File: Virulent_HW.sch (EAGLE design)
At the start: 6 parts

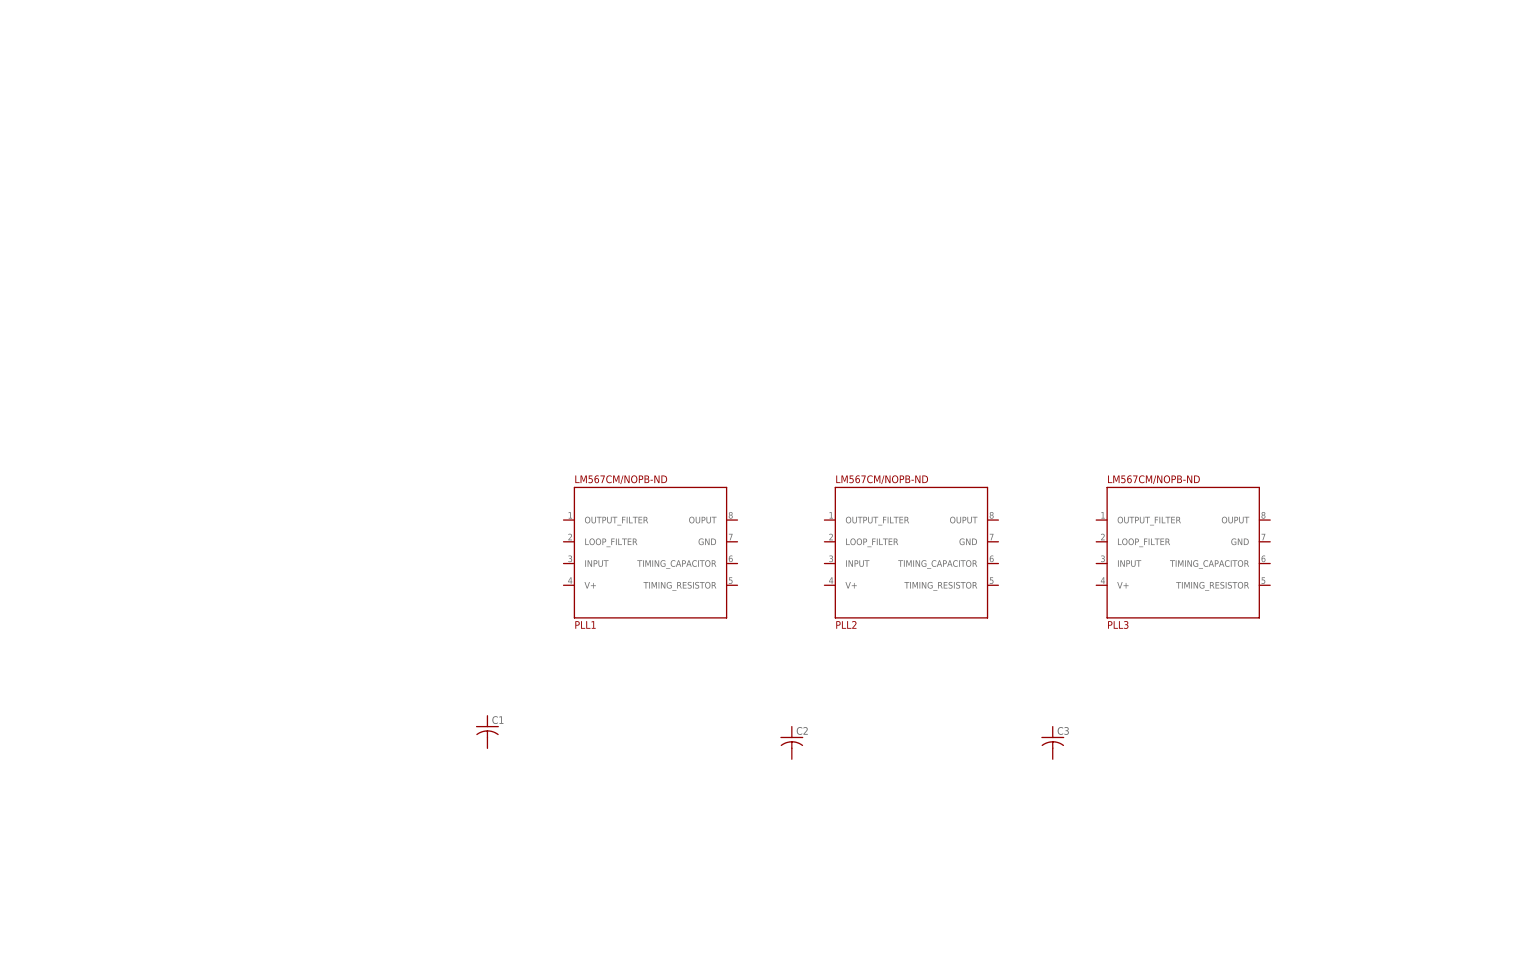
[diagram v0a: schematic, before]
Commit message: Added datasheets folder. Added power supply to schematic.
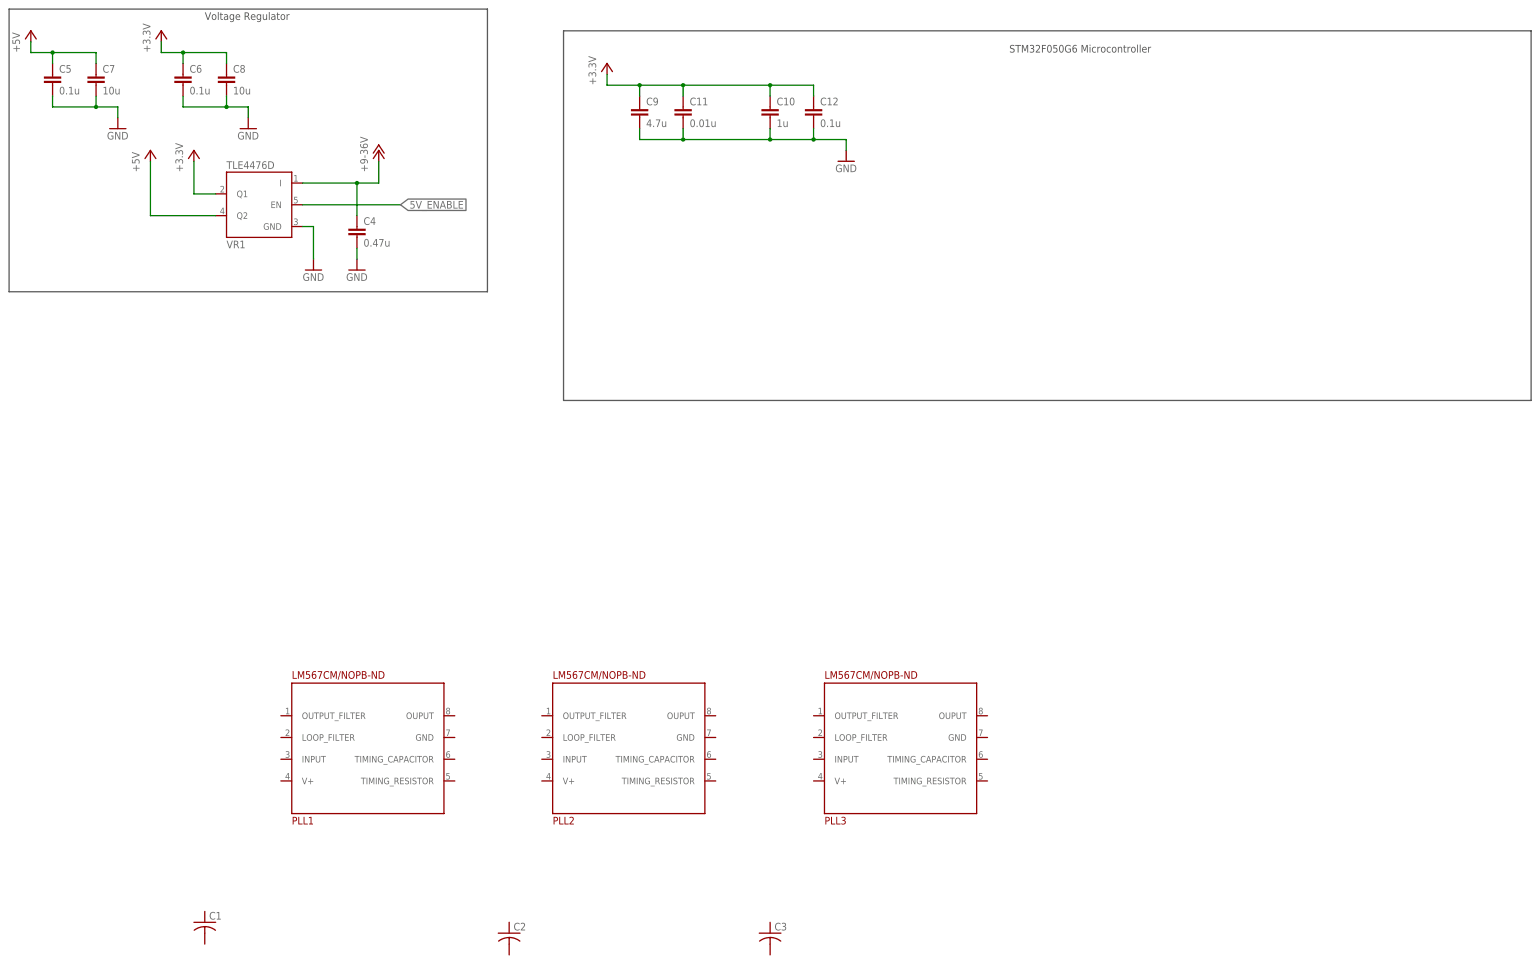
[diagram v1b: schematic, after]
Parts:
- added C10: 1u, rcl:C-EUC0805
- added C11: 0.01u, rcl:C-EUC0402
- added C12, C5, C6: 0.1u, rcl:C-EUC0402
- added C4: 0.47u, rcl:C-EUC1206
- added C7, C8: 10u, rcl:C-EUC1206
- added C9: 4.7u, rcl:C-EUC0805
- added VR1: TLE4476D, motorFeedback:TLE4476D
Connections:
- new net +3.3V: C10.1, C11.1, C12.1, C6.1, C8.1, C9.1, VR1.Q1@2
- new net +5V: C5.1, C7.1, VR1.Q2@4
- new net +9-36V: C4.1, VR1.I@1
- new net 5V_ENABLE: VR1.EN@5
- new net GND: C10.2, C11.2, C12.2, C4.2, C5.2, C6.2, C7.2, C8.2, C9.2, VR1.GND@3
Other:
- note added: "STM32F050G6 Microcontroller"
- note added: "Voltage Regulator"
- moved on the sheet: C1, C2, C3, PLL1, PLL2, PLL3

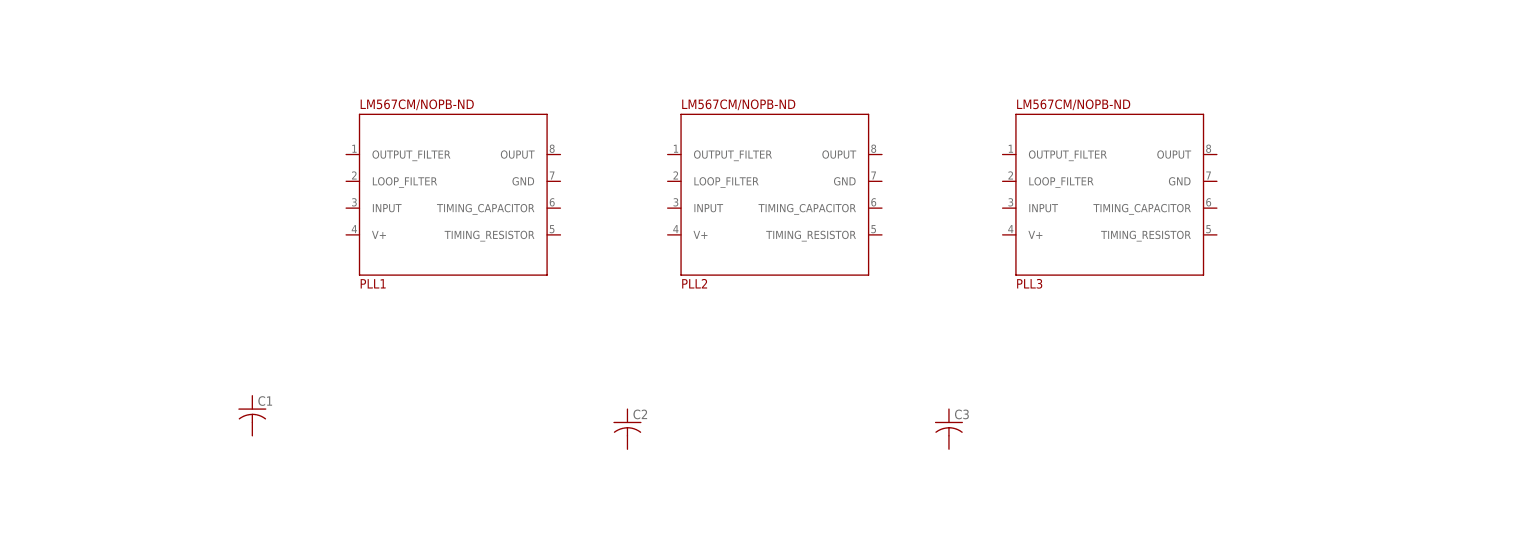
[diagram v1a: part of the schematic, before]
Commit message: Added RGB LED (MSL0201RGB) and Hex Inverter (SN74ACT14) to library. Updated PLL circuitry in schematic.
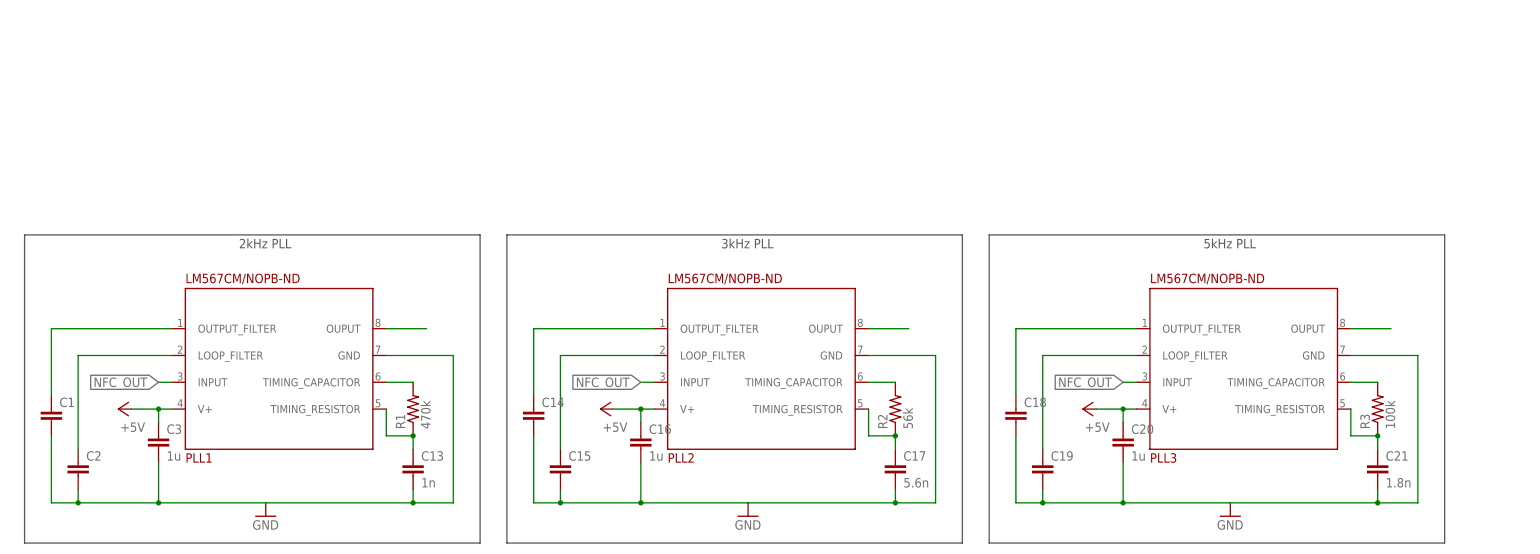
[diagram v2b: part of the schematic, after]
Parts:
- added C13: 1n, rcl:C-EUC1206
- added C14, C15, C18, C19: (no value), rcl:C-EUC1206
- added C16, C20: 1u, rcl:C-EUC1206
- added C17: 5.6n, rcl:C-EUC1206
- added C21: 1.8n, rcl:C-EUC1206
- added R1: 470k, Virulent_HW:R-US_R0402
- added R2: 56k, Virulent_HW:R-US_R0402
- added R3: 100k, Virulent_HW:R-US_R0402
- C1, C2: device rcl:C-USC0805 -> rcl:C-EUC1206
- C3: value (none) -> 1u; device rcl:C-USC0805 -> rcl:C-EUC1206
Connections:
- new net N$1: C1.1, PLL1.OUTPUT_FILTER@1
- new net N$10: C17.1, PLL2.TIMING_RESISTOR@5, R2.1
- new net N$12: C18.1, PLL3.OUTPUT_FILTER@1
- new net N$13: PLL3.TIMING_CAPACITOR@6, R3.2
- new net N$14: C19.1, PLL3.LOOP_FILTER@2
- new net N$15: PLL3.OUPUT@8
- new net N$17: C21.1, PLL3.TIMING_RESISTOR@5, R3.1
- new net N$2: C14.1, PLL2.OUTPUT_FILTER@1
- new net N$3: PLL1.TIMING_CAPACITOR@6, R1.2
- new net N$4: C13.1, PLL1.TIMING_RESISTOR@5, R1.1
- new net N$5: C2.1, PLL1.LOOP_FILTER@2
- new net N$6: PLL1.OUPUT@8
- new net N$7: PLL2.TIMING_CAPACITOR@6, R2.2
- new net N$8: C15.1, PLL2.LOOP_FILTER@2
- new net N$9: PLL2.OUPUT@8
- new net NFC_OUT: PLL1.INPUT@3, PLL2.INPUT@3, PLL3.INPUT@3
- net +5V: now also C16.1, C20.1, C3.1, PLL1.V+@4, PLL2.V+@4, PLL3.V+@4
- net GND: now also C1.2, C13.2, C14.2, C15.2, C16.2, C17.2, C18.2, C19.2, C2.2, C20.2, C21.2, C3.2, PLL1.GND@7, PLL2.GND@7, PLL3.GND@7
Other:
- note added: "2kHz PLL"
- note added: "3kHz PLL"
- note added: "5kHz PLL"
- moved on the sheet: C1, C2, C3, PLL1, PLL2, PLL3
